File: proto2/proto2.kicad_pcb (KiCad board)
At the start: 2 copper layers, 187.5 x 109.8 mm, 182 parts, among them J1 Output 1, J10 Output, J11 Device, J12 Daughter Card, J2 Main Power, J3 Output, J4 Output, J5 Device, J6 Output, J7 Device, J8 Output, J9 Device, SW1 SW_DIP_x04, U1 AQY282SX, U10 AQY282SX, U11 AQY282SX, U12 AQY282SX, U13 LDO, U2 AQY282SX, U3 AQY282SX, U4 AQY282SX, U5 AQY282SX, U6 AQY282SX, U7 AQY282SX, U8 AQY282SX, U9 AQY282SX

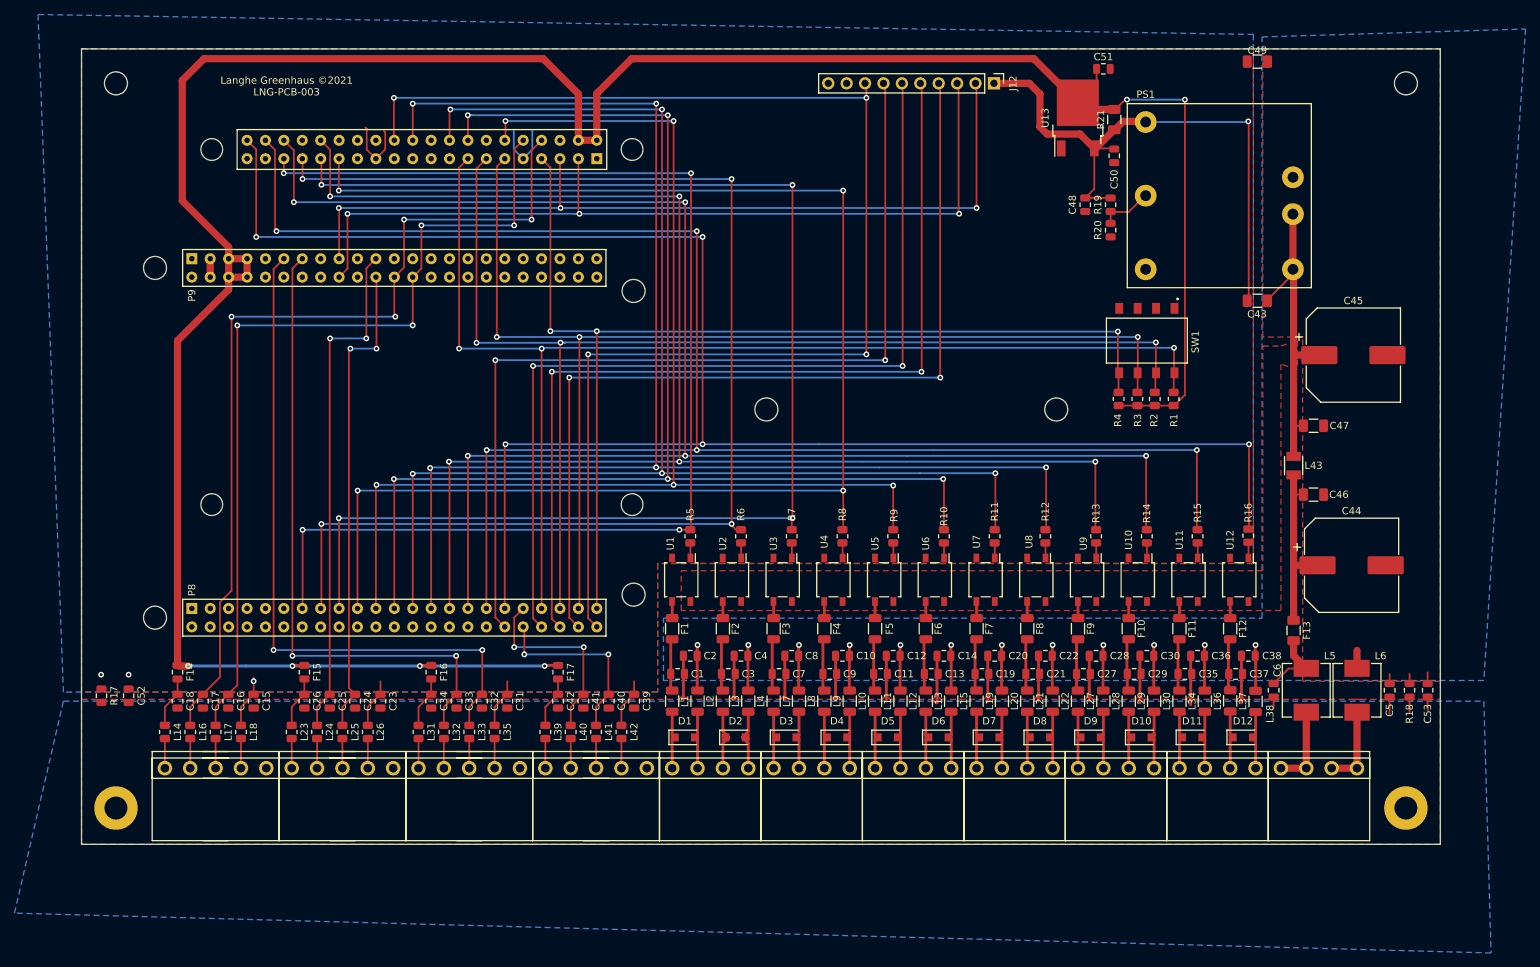
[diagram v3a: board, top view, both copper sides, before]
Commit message: Reversed the filter order.
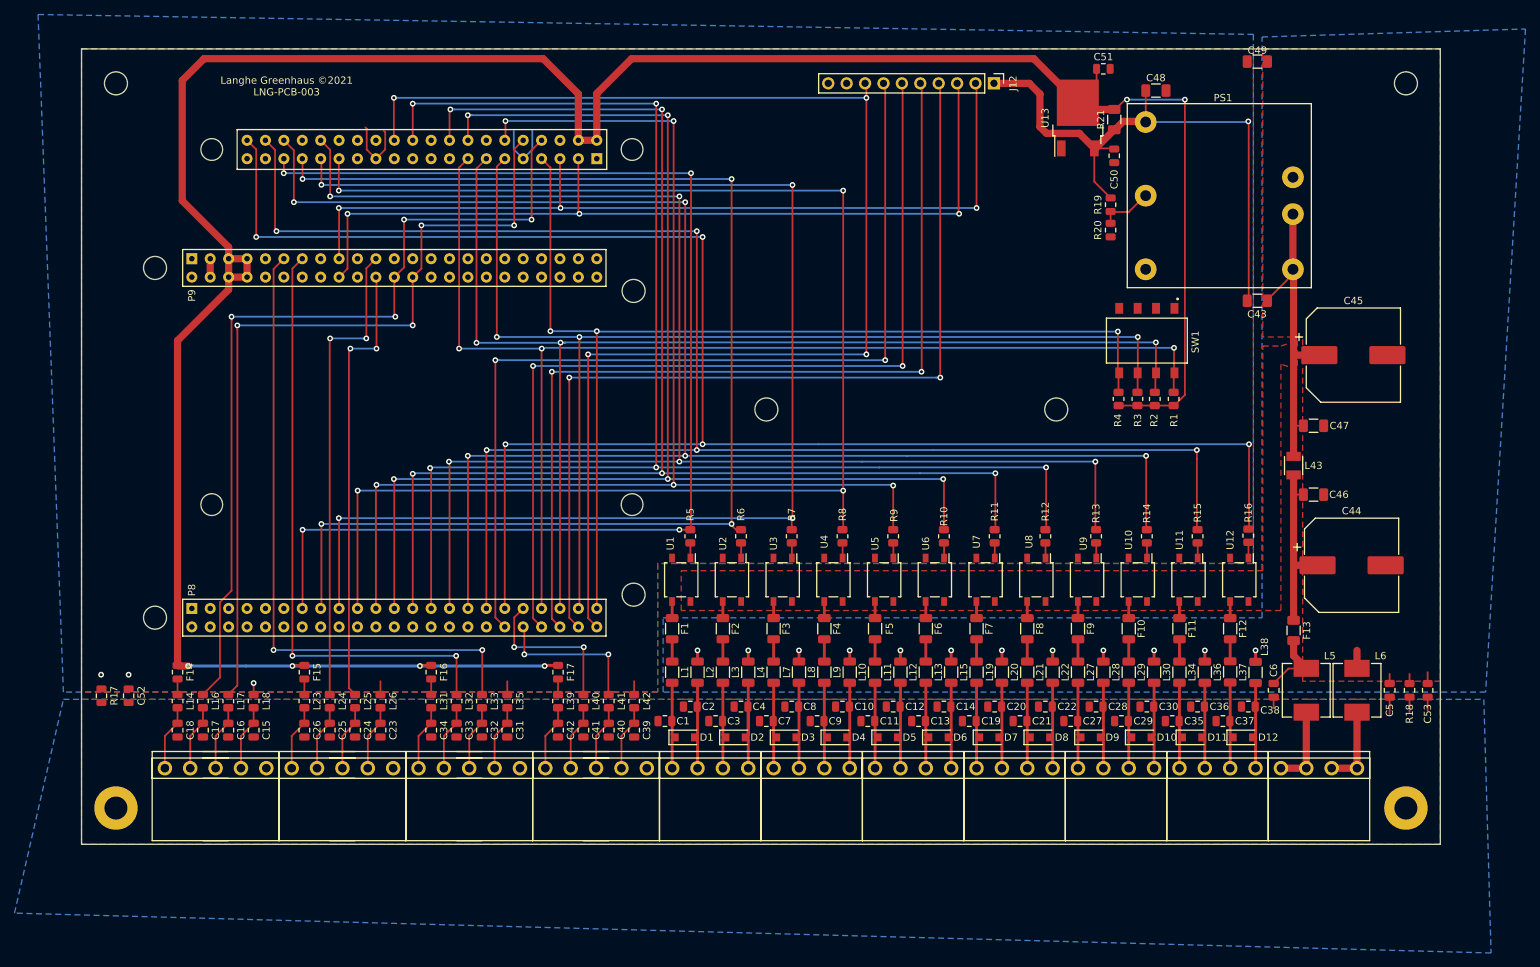
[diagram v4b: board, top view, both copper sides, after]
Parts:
- C48: footprint Capacitor_SMD:C_0805_2012Metric -> Capacitor_SMD:C_1206_3216Metric
- moved C48 18.5 mm to (178.8, 59.0), turned to 0 degrees
- moved C10 7.00 mm to (135.5, 144.0)
- moved C12 7.00 mm to (142.5, 144.0)
- moved C14 7.00 mm to (149.5, 144.0)
- moved C2 7.00 mm to (114.5, 144.0)
- moved C20 7.00 mm to (156.5, 144.0)
- moved C22 7.00 mm to (163.5, 144.0)
- moved C28 7.00 mm to (170.5, 144.0)
- moved C30 7.00 mm to (177.5, 144.0)
- moved C36 7.00 mm to (184.5, 144.0)
- moved C38 7.00 mm to (191.5, 144.0)
- moved C4 7.00 mm to (121.5, 144.0)
- moved C8 7.00 mm to (128.5, 144.0)
- moved C1 6.73 mm to (111.0, 146.0), turned to 180 degrees
- moved C11 6.73 mm to (139.0, 146.0), turned to 180 degrees
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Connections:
- C1 pad 1: DQ1_1 -> Net-(C1-Pad1)
- C10 pad 1: Earth -> Net-(C10-Pad1)
- C11 pad 1: DQ3_1 -> Net-(C11-Pad1)
- C12 pad 1: Earth -> Net-(C12-Pad1)
- C13 pad 1: DQ3_2 -> Net-(C13-Pad1)
- C14 pad 1: Earth -> Net-(C14-Pad1)
- C15 pad 1: GND -> Net-(C15-Pad1)
- C16 pad 1: RX_1 -> Net-(C16-Pad1)
- C17 pad 1: TX_1 -> Net-(C17-Pad1)
- C18 pad 1: 5V_1 -> Net-(C18-Pad1)
- C19 pad 1: DQ4_1 -> Net-(C19-Pad1)
- C2 pad 1: Earth -> Net-(C2-Pad1)
- C20 pad 1: Earth -> Net-(C20-Pad1)
- C21 pad 1: DQ4_2 -> Net-(C21-Pad1)
- C22 pad 1: Earth -> Net-(C22-Pad1)
- C23 pad 1: GND -> Net-(C23-Pad1)
- C24 pad 1: RX_2 -> Net-(C24-Pad1)
- C25 pad 1: TX_2 -> Net-(C25-Pad1)
- C26 pad 1: 5V_2 -> Net-(C26-Pad1)
- C27 pad 1: DQ5_1 -> Net-(C27-Pad1)
- C28 pad 1: Earth -> Net-(C28-Pad1)
- C29 pad 1: DQ5_2 -> Net-(C29-Pad1)
- C3 pad 1: DQ1_2 -> Net-(C3-Pad1)
- C30 pad 1: Earth -> Net-(C30-Pad1)
- C31 pad 1: GND -> Net-(C31-Pad1)
- C32 pad 1: RX_3 -> Net-(C32-Pad1)
- C33 pad 1: TX_3 -> Net-(C33-Pad1)
- C34 pad 1: 5V_3 -> Net-(C34-Pad1)
- C35 pad 1: DQ6_1 -> Net-(C35-Pad1)
- C36 pad 1: Earth -> Net-(C36-Pad1)
- C37 pad 1: DQ6_2 -> Net-(C37-Pad1)
- C38 pad 1: Earth -> Net-(C38-Pad1)
- C39 pad 1: GND -> Net-(C39-Pad1)
- C4 pad 1: Earth -> Net-(C4-Pad1)
- C40 pad 1: RX_4 -> Net-(C40-Pad1)
- C41 pad 1: TX_4 -> Net-(C41-Pad1)
- C42 pad 1: 5V_4 -> Net-(C42-Pad1)
- C7 pad 1: DQ2_1 -> Net-(C7-Pad1)
- C8 pad 1: Earth -> Net-(C8-Pad1)
- C9 pad 1: DQ2_2 -> Net-(C9-Pad1)
- D1 pad 1: Net-(D1-Pad1) -> Net-(C1-Pad1)
- D1 pad 2: Net-(D1-Pad2) -> Net-(C2-Pad1)
- D10 pad 1: Net-(D10-Pad1) -> Net-(C29-Pad1)
- D10 pad 2: Net-(D10-Pad2) -> Net-(C30-Pad1)
- D11 pad 1: Net-(D11-Pad1) -> Net-(C35-Pad1)
- D11 pad 2: Net-(D11-Pad2) -> Net-(C36-Pad1)
- D12 pad 1: Net-(D12-Pad1) -> Net-(C37-Pad1)
- D12 pad 2: Net-(D12-Pad2) -> Net-(C38-Pad1)
- D2 pad 1: Net-(D2-Pad1) -> Net-(C3-Pad1)
- D2 pad 2: Net-(D2-Pad2) -> Net-(C4-Pad1)
- D3 pad 1: Net-(D3-Pad1) -> Net-(C7-Pad1)
- D3 pad 2: Net-(D3-Pad2) -> Net-(C8-Pad1)
- D4 pad 1: Net-(D4-Pad1) -> Net-(C9-Pad1)
- D4 pad 2: Net-(D4-Pad2) -> Net-(C10-Pad1)
- D5 pad 1: Net-(D5-Pad1) -> Net-(C11-Pad1)
- D5 pad 2: Net-(D5-Pad2) -> Net-(C12-Pad1)
- D6 pad 1: Net-(D6-Pad1) -> Net-(C13-Pad1)
- D6 pad 2: Net-(D6-Pad2) -> Net-(C14-Pad1)
- D7 pad 1: Net-(D7-Pad1) -> Net-(C19-Pad1)
- D7 pad 2: Net-(D7-Pad2) -> Net-(C20-Pad1)
- D8 pad 1: Net-(D8-Pad1) -> Net-(C21-Pad1)
- D8 pad 2: Net-(D8-Pad2) -> Net-(C22-Pad1)
- D9 pad 1: Net-(D9-Pad1) -> Net-(C27-Pad1)
- D9 pad 2: Net-(D9-Pad2) -> Net-(C28-Pad1)
- J1 pad 1: Net-(D1-Pad1) -> Net-(C1-Pad1)
- J1 pad 2: Net-(D1-Pad2) -> Net-(C2-Pad1)
- J1 pad 3: Net-(D2-Pad1) -> Net-(C3-Pad1)
- J1 pad 4: Net-(D2-Pad2) -> Net-(C4-Pad1)
- J10 pad 1: Net-(D11-Pad1) -> Net-(C35-Pad1)
- J10 pad 2: Net-(D11-Pad2) -> Net-(C36-Pad1)
- J10 pad 3: Net-(D12-Pad1) -> Net-(C37-Pad1)
- J10 pad 4: Net-(D12-Pad2) -> Net-(C38-Pad1)
- J11 pad 1: Net-(J11-Pad1) -> Net-(C42-Pad1)
- J11 pad 2: Net-(J11-Pad2) -> Net-(C41-Pad1)
- J11 pad 3: Net-(J11-Pad3) -> Net-(C40-Pad1)
- J11 pad 4: Net-(J11-Pad4) -> Net-(C39-Pad1)
- J3 pad 1: Net-(D3-Pad1) -> Net-(C7-Pad1)
- J3 pad 2: Net-(D3-Pad2) -> Net-(C8-Pad1)
- J3 pad 3: Net-(D4-Pad1) -> Net-(C9-Pad1)
- J3 pad 4: Net-(D4-Pad2) -> Net-(C10-Pad1)
- J4 pad 1: Net-(D5-Pad1) -> Net-(C11-Pad1)
- J4 pad 2: Net-(D5-Pad2) -> Net-(C12-Pad1)
- J4 pad 3: Net-(D6-Pad1) -> Net-(C13-Pad1)
- J4 pad 4: Net-(D6-Pad2) -> Net-(C14-Pad1)
- J5 pad 1: Net-(J5-Pad1) -> Net-(C18-Pad1)
- J5 pad 2: Net-(J5-Pad2) -> Net-(C17-Pad1)
- J5 pad 3: Net-(J5-Pad3) -> Net-(C16-Pad1)
- J5 pad 4: Net-(J5-Pad4) -> Net-(C15-Pad1)
- J6 pad 1: Net-(D7-Pad1) -> Net-(C19-Pad1)
- J6 pad 2: Net-(D7-Pad2) -> Net-(C20-Pad1)
- J6 pad 3: Net-(D8-Pad1) -> Net-(C21-Pad1)
- J6 pad 4: Net-(D8-Pad2) -> Net-(C22-Pad1)
- J7 pad 1: Net-(J7-Pad1) -> Net-(C26-Pad1)
- J7 pad 2: Net-(J7-Pad2) -> Net-(C25-Pad1)
- J7 pad 3: Net-(J7-Pad3) -> Net-(C24-Pad1)
- J7 pad 4: Net-(J7-Pad4) -> Net-(C23-Pad1)
- J8 pad 1: Net-(D9-Pad1) -> Net-(C27-Pad1)
- J8 pad 2: Net-(D9-Pad2) -> Net-(C28-Pad1)
- J8 pad 3: Net-(D10-Pad1) -> Net-(C29-Pad1)
- J8 pad 4: Net-(D10-Pad2) -> Net-(C30-Pad1)
- J9 pad 1: Net-(J9-Pad1) -> Net-(C34-Pad1)
- J9 pad 2: Net-(J9-Pad2) -> Net-(C33-Pad1)
- J9 pad 3: Net-(J9-Pad3) -> Net-(C32-Pad1)
- J9 pad 4: Net-(J9-Pad4) -> Net-(C31-Pad1)
- L1 pad 2: Net-(D1-Pad1) -> Net-(C1-Pad1)
- L10 pad 2: Net-(D4-Pad2) -> Net-(C10-Pad1)
- L11 pad 2: Net-(D5-Pad1) -> Net-(C11-Pad1)
- L12 pad 2: Net-(D5-Pad2) -> Net-(C12-Pad1)
- L13 pad 2: Net-(D6-Pad1) -> Net-(C13-Pad1)
- L14 pad 2: Net-(J5-Pad1) -> Net-(C18-Pad1)
- L15 pad 2: Net-(D6-Pad2) -> Net-(C14-Pad1)
- L16 pad 2: Net-(J5-Pad2) -> Net-(C17-Pad1)
- L17 pad 2: Net-(J5-Pad3) -> Net-(C16-Pad1)
- L18 pad 2: Net-(J5-Pad4) -> Net-(C15-Pad1)
- L19 pad 2: Net-(D7-Pad1) -> Net-(C19-Pad1)
- L2 pad 2: Net-(D1-Pad2) -> Net-(C2-Pad1)
- L20 pad 2: Net-(D7-Pad2) -> Net-(C20-Pad1)
- L21 pad 2: Net-(D8-Pad1) -> Net-(C21-Pad1)
- L22 pad 2: Net-(D8-Pad2) -> Net-(C22-Pad1)
- L23 pad 2: Net-(J7-Pad1) -> Net-(C26-Pad1)
- L24 pad 2: Net-(J7-Pad2) -> Net-(C25-Pad1)
- L25 pad 2: Net-(J7-Pad3) -> Net-(C24-Pad1)
- L26 pad 2: Net-(J7-Pad4) -> Net-(C23-Pad1)
- L27 pad 2: Net-(D9-Pad1) -> Net-(C27-Pad1)
- L28 pad 2: Net-(D9-Pad2) -> Net-(C28-Pad1)
- L29 pad 2: Net-(D10-Pad1) -> Net-(C29-Pad1)
- L3 pad 2: Net-(D2-Pad1) -> Net-(C3-Pad1)
- L30 pad 2: Net-(D10-Pad2) -> Net-(C30-Pad1)
- L31 pad 2: Net-(J9-Pad1) -> Net-(C34-Pad1)
- L32 pad 2: Net-(J9-Pad2) -> Net-(C33-Pad1)
- L33 pad 2: Net-(J9-Pad3) -> Net-(C32-Pad1)
- L34 pad 2: Net-(D11-Pad1) -> Net-(C35-Pad1)
- L35 pad 2: Net-(J9-Pad4) -> Net-(C31-Pad1)
- L36 pad 2: Net-(D11-Pad2) -> Net-(C36-Pad1)
- L37 pad 2: Net-(D12-Pad1) -> Net-(C37-Pad1)
- L38 pad 2: Net-(D12-Pad2) -> Net-(C38-Pad1)
- L39 pad 2: Net-(J11-Pad1) -> Net-(C42-Pad1)
- L4 pad 2: Net-(D2-Pad2) -> Net-(C4-Pad1)
- L40 pad 2: Net-(J11-Pad2) -> Net-(C41-Pad1)
- L41 pad 2: Net-(J11-Pad3) -> Net-(C40-Pad1)
- L42 pad 2: Net-(J11-Pad4) -> Net-(C39-Pad1)
- L7 pad 2: Net-(D3-Pad1) -> Net-(C7-Pad1)
- L8 pad 2: Net-(D3-Pad2) -> Net-(C8-Pad1)
- L9 pad 2: Net-(D4-Pad1) -> Net-(C9-Pad1)
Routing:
- net GNDPWR: track 86.2 -> 7.73 mm
- net Earth: track 82.7 -> 25.1 mm
- net GND: track 46.0 -> 25.3 mm
- net Net-(C4-Pad1): track 0.00 -> 16.3 mm
- net Net-(C3-Pad1): track 0.00 -> 12.3 mm
- net Net-(C37-Pad1): track 0.00 -> 12.1 mm
- net Net-(C9-Pad1): track 0.00 -> 12.1 mm
- net Net-(C8-Pad1): track 0.00 -> 12.1 mm
- net Net-(C7-Pad1): track 0.00 -> 12.1 mm
- net Net-(C36-Pad1): track 0.00 -> 12.1 mm
- net Net-(C35-Pad1): track 0.00 -> 12.1 mm
- net Net-(C30-Pad1): track 0.00 -> 12.1 mm
- net Net-(C29-Pad1): track 0.00 -> 12.1 mm
- net Net-(C28-Pad1): track 0.00 -> 12.1 mm
- net Net-(C27-Pad1): track 0.00 -> 12.1 mm
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
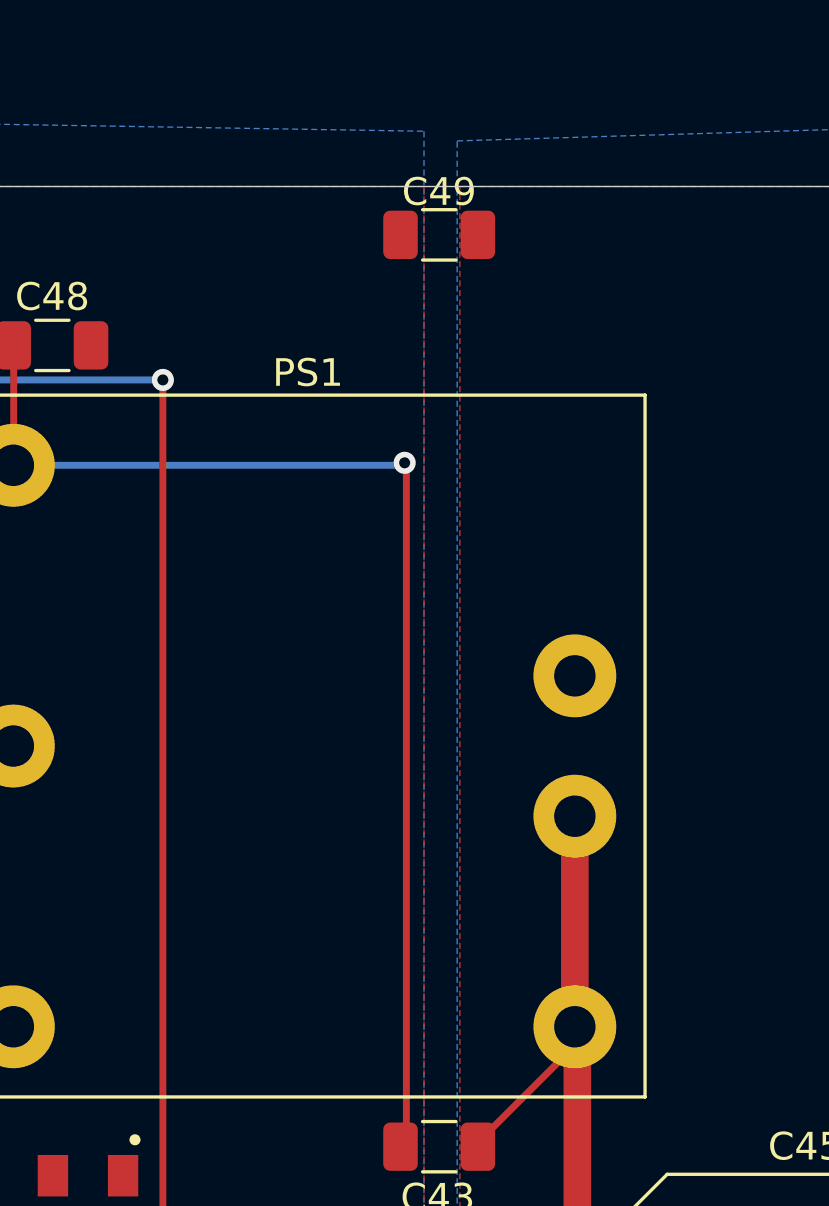
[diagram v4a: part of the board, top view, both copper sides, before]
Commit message: Updated filters and Power supply foorptint.
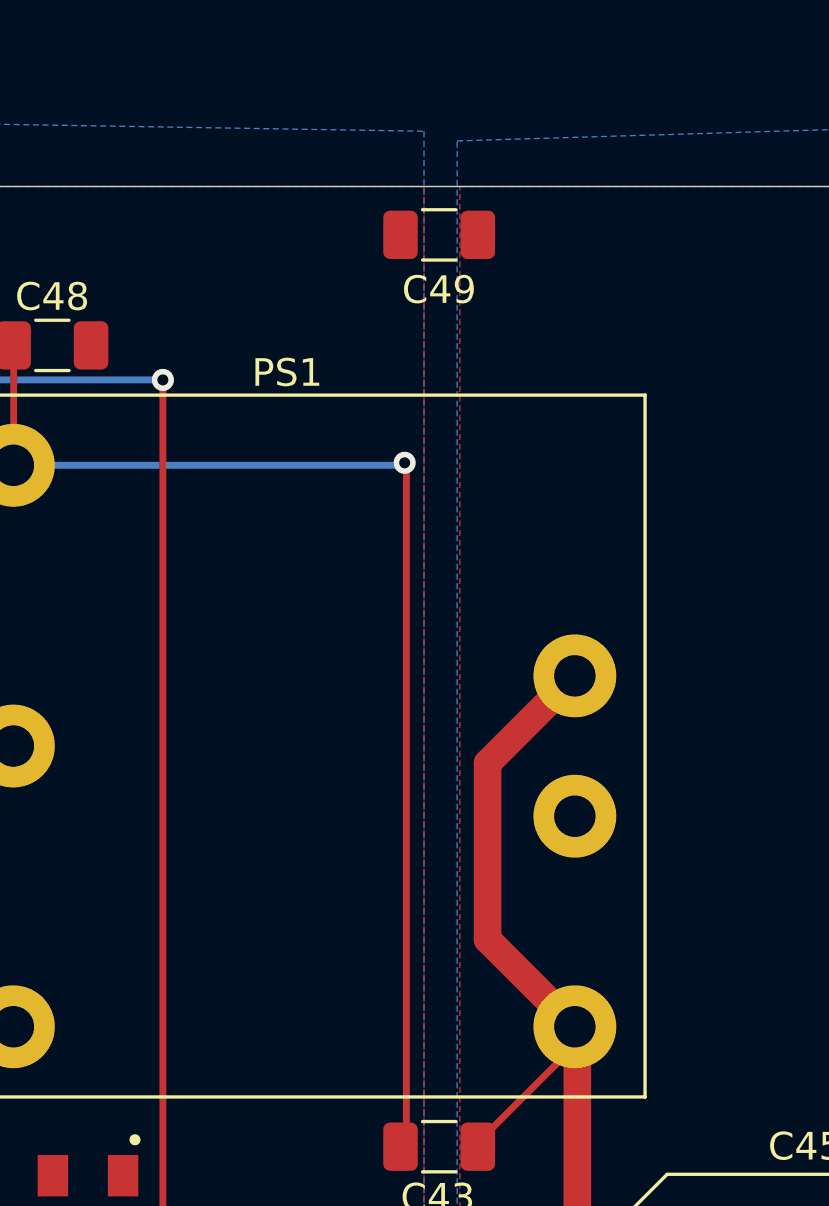
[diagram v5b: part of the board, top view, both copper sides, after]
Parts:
- PS1: value CUI PDQE20 -> CUI_PDQE20_ISOLATED_DCDC
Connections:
- PS1 pad 2: VDQ1 -> Earth
- PS1 pad 3: Earth -> VDQ1
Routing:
- net VDQ1: track 42.8 -> 50.5 mm
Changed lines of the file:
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@@
     (thickness 1.6)
     (drawings 37)
-    (tracks 816)
+    (tracks 818)
     (zones 0)
     (modules 182)
@@
   )
   (setup
-    (last_trace_width 0.25)
+    (last_trace_width 1)
     (user_trace_width 0.4)
     (user_trace_width 1)
@@
     (add_net VIN)
   )
+  (module Converter_BCR:CUI_PDQE20 (layer F.Cu)
+    (at 187.5 73.5 180)
+    (fp_text reference PS1 (at 0.25 13.5) (layer F.SilkS)
+      (effects (font (size 1 1) (thickness 0.15)))
+    )
+    (fp_text value CUI_PDQE20_ISOLATED_DCDC (at 0 -15.24) (layer F.Fab)
+      (effects (font (size 1 1) (thickness 0.15)))
+    )
+    (fp_line (start 12.7 -12.7) (end -12.7 -12.7) (layer F.SilkS) (width 0.12))
+    (fp_line (start 12.7 12.7) (end 12.7 -12.7) (layer F.SilkS) (width 0.12))
+    (fp_line (start -12.7 12.7) (end 12.7 12.7) (layer F.SilkS) (width 0.12))
+    (fp_line (start -12.7 -12.7) (end -12.7 12.7) (layer F.SilkS) (width 0.12))
+    (pad 6 thru_hole circle (at 10.16 -10.16 180) (size 3 3) (drill 1.5) (layers *.Cu *.Mask)
+      (net 22 GND))
+    (pad 5 thru_hole circle (at 10.16 0 180) (size 3 3) (drill 1.5) (layers *.Cu *.Mask)
+      (net 126 /Power/TRIM))
+    (pad 4 thru_hole circle (at 10.16 10.16 180) (size 3 3) (drill 1.5) (layers *.Cu *.Mask)
+      (net 111 VDD))
+    (pad 3 thru_hole circle (at -10.16 2.54 180) (size 3 3) (drill 1.5) (layers *.Cu *.Mask)
+      (net 127 VDQ1))
+    (pad 2 thru_hole circle (at -10.16 -2.54 180) (size 3 3) (drill 1.5) (layers *.Cu *.Mask)
+      (net 89 Earth))
+    (pad 1 thru_hole circle (at -10.16 -10.16 180) (size 3 3) (drill 1.5) (layers *.Cu *.Mask)
+      (net 127 VDQ1))
+  )
   (module Capacitor_SMD:C_1206_3216Metric (layer F.Cu)
     (at 178.75 59)
@@
     (tags capacitor)
     (attr smd)
-    (fp_text reference C49 (at 0 -1.55) (layer F.SilkS)
+    (fp_text reference C49 (at 0 2) (layer F.SilkS)
       (effects (font (size 1 1) (thickness 0.15)))
     )
@@
     )
   )
-  (module Converter_BCR:CUI_PDQE20 (layer F.Cu)
-    (at 187.5 73.5 180)
-    (fp_text reference PS1 (at -0.5 13.5) (layer F.SilkS)
-      (effects (font (size 1 1) (thickness 0.15)))
-    )
-    (fp_text value "CUI PDQE20" (at 0 -15.24) (layer F.Fab)
-      (effects (font (size 1 1) (thickness 0.15)))
-    )
-    (fp_line (start 12.7 -12.7) (end -12.7 -12.7) (layer F.SilkS) (width 0.12))
-    (fp_line (start 12.7 12.7) (end 12.7 -12.7) (layer F.SilkS) (width 0.12))
-    (fp_line (start -12.7 12.7) (end 12.7 12.7) (layer F.SilkS) (width 0.12))
-    (fp_line (start -12.7 -12.7) (end -12.7 12.7) (layer F.SilkS) (width 0.12))
-    (pad 6 thru_hole circle (at 10.16 -10.16 180) (size 3 3) (drill 1.5) (layers *.Cu *.Mask)
-      (net 22 GND))
-    (pad 5 thru_hole circle (at 10.16 0 180) (size 3 3) (drill 1.5) (layers *.Cu *.Mask)
-      (net 126 /Power/TRIM))
-    (pad 4 thru_hole circle (at 10.16 10.16 180) (size 3 3) (drill 1.5) (layers *.Cu *.Mask)
-      (net 111 VDD))
-    (pad 3 thru_hole circle (at -10.16 2.54 180) (size 3 3) (drill 1.5) (layers *.Cu *.Mask)
-      (net 89 Earth))
-    (pad 2 thru_hole circle (at -10.16 -2.54 180) (size 3 3) (drill 1.5) (layers *.Cu *.Mask)
-      (net 127 VDQ1))
-    (pad 1 thru_hole circle (at -10.16 -10.16 180) (size 3 3) (drill 1.5) (layers *.Cu *.Mask)
-      (net 127 VDQ1))
-  )
   (module Inductor_BCR:Murata_LQH32PN2R2NN0L (layer F.Cu)
     (at 197.75 110.75 90)
@@
   (segment (start 197.66 84.34) (end 194.25 87.75) (width 0.25) (layer F.Cu) (net 127))
   (segment (start 197.66 83.66) (end 197.66 84.34) (width 0.25) (layer F.Cu) (net 127))
-  (segment (start 197.66 76.04) (end 197.66 83.66) (width 1) (layer F.Cu) (net 127))
+  (segment (start 194.5 74.12) (end 197.66 70.96) (width 1) (layer F.Cu) (net 127))
+  (segment (start 194.5 80.5) (end 194.5 74.12) (width 1) (layer F.Cu) (net 127))
+  (segment (start 197.66 83.66) (end 194.5 80.5) (width 1) (layer F.Cu) (net 127))
   (segment (start 112 148.6) (end 112.35 148.25) (width 0.4) (layer F.Cu) (net 137))
   (segment (start 112 152.5) (end 112 148.6) (width 0.4) (layer F.Cu) (net 137))
